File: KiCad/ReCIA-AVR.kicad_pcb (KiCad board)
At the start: 4 copper layers, 17.4 x 51.4 mm, 9 parts, among them U1 AVR128DA64-I_MR, U2 74AHCT1G17, U5 8520_DIP

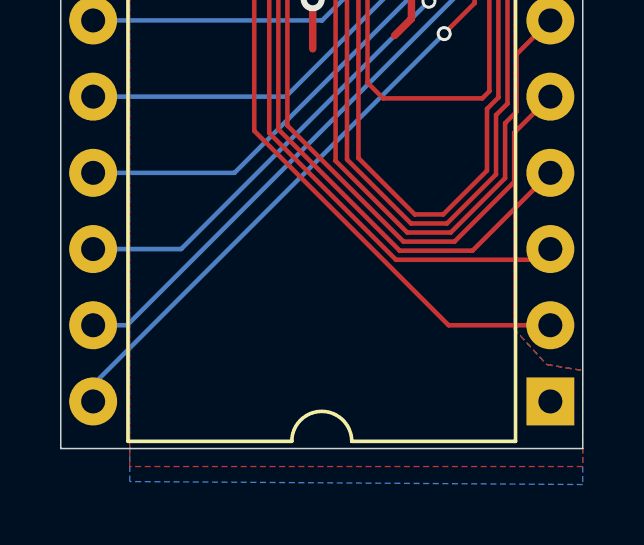
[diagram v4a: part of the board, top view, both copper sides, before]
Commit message: Add TLC2932AIPWR to the AVR version
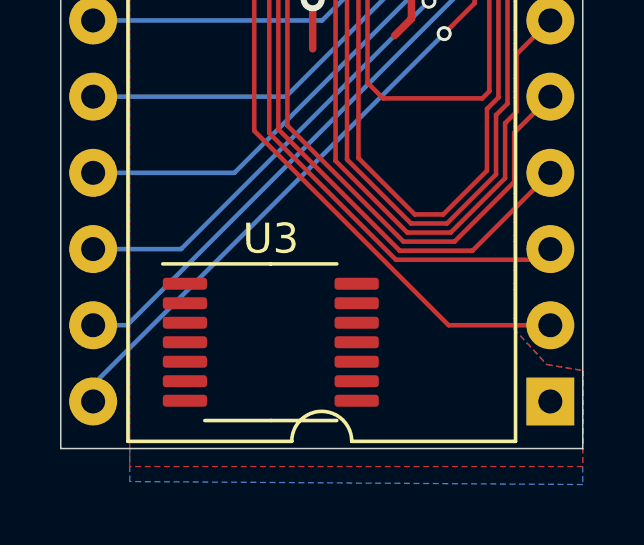
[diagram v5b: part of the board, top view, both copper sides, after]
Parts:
- added U3: TLC2932AIPWR, Package_SO:TSSOP-14_4.4x5mm_P0.65mm, F.Cu at (130.3, 105.2)
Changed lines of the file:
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@@
     (tracks 377)
     (zones 0)
-    (modules 9)
-    (nets 62)
+    (modules 10)
+    (nets 76)
   )
   (page A4)
@@
   (net 60 E)
   (net 61 /ECLK)
+  (net 62 "Net-(U3-Pad14)")
+  (net 63 "Net-(U3-Pad13)")
+  (net 64 "Net-(U3-Pad12)")
+  (net 65 "Net-(U3-Pad11)")
+  (net 66 "Net-(U3-Pad10)")
+  (net 67 "Net-(U3-Pad9)")
+  (net 68 "Net-(U3-Pad8)")
+  (net 69 "Net-(U3-Pad7)")
+  (net 70 "Net-(U3-Pad6)")
+  (net 71 "Net-(U3-Pad5)")
+  (net 72 "Net-(U3-Pad4)")
+  (net 73 "Net-(U3-Pad3)")
+  (net 74 "Net-(U3-Pad2)")
+  (net 75 "Net-(U3-Pad1)")
   (net_class Default "This is the default net class."
     (clearance 0.15)
@@
     (add_net "Net-(U1-Pad5)")
     (add_net "Net-(U2-Pad1)")
+    (add_net "Net-(U3-Pad1)")
+    (add_net "Net-(U3-Pad10)")
+    (add_net "Net-(U3-Pad11)")
+    (add_net "Net-(U3-Pad12)")
+    (add_net "Net-(U3-Pad13)")
+    (add_net "Net-(U3-Pad14)")
+    (add_net "Net-(U3-Pad2)")
+    (add_net "Net-(U3-Pad3)")
+    (add_net "Net-(U3-Pad4)")
+    (add_net "Net-(U3-Pad5)")
+    (add_net "Net-(U3-Pad6)")
+    (add_net "Net-(U3-Pad7)")
+    (add_net "Net-(U3-Pad8)")
+    (add_net "Net-(U3-Pad9)")
     (add_net PA0)
     (add_net PA1)
@@
     (add_net XTAL32K2)
   )
+  (module Package_SO:TSSOP-14_4.4x5mm_P0.65mm (layer F.Cu)
+    (at 130.302 105.156)
+    (descr "TSSOP, 14 Pin (JEDEC MO-153 Var AB-1 https://www.jedec.org/document_search?search_api_views_fulltext=MO-153), generated with kicad-footprint-generator ipc_gullwing_generator.py")
+    (tags "TSSOP SO")
+    (attr smd)
+    (fp_text reference U3 (at 0 -3.45) (layer F.SilkS)
+      (effects (font (size 1 1) (thickness 0.15)))
+    )
+    (fp_text value TLC2932AIPWR (at 0 3.45) (layer F.Fab) hide
+      (effects (font (size 1 1) (thickness 0.15)))
+    )
+    (fp_text user %R (at 0 0) (layer F.Fab) hide
+      (effects (font (size 1 1) (thickness 0.15)))
+    )
+    (fp_line (start 0 2.61) (end 2.2 2.61) (layer F.SilkS) (width 0.12))
+    (fp_line (start 0 2.61) (end -2.2 2.61) (layer F.SilkS) (width 0.12))
+    (fp_line (start 0 -2.61) (end 2.2 -2.61) (layer F.SilkS) (width 0.12))
+    (fp_line (start 0 -2.61) (end -3.6 -2.61) (layer F.SilkS) (width 0.12))
+    (fp_line (start -1.2 -2.5) (end 2.2 -2.5) (layer F.Fab) (width 0.1))
+    (fp_line (start 2.2 -2.5) (end 2.2 2.5) (layer F.Fab) (width 0.1))
+    (fp_line (start 2.2 2.5) (end -2.2 2.5) (layer F.Fab) (width 0.1))
+    (fp_line (start -2.2 2.5) (end -2.2 -1.5) (layer F.Fab) (width 0.1))
+    (fp_line (start -2.2 -1.5) (end -1.2 -2.5) (layer F.Fab) (width 0.1))
+    (fp_line (start -3.85 -2.75) (end -3.85 2.75) (layer F.CrtYd) (width 0.05))
+    (fp_line (start -3.85 2.75) (end 3.85 2.75) (layer F.CrtYd) (width 0.05))
+    (fp_line (start 3.85 2.75) (end 3.85 -2.75) (layer F.CrtYd) (width 0.05))
+    (fp_line (start 3.85 -2.75) (end -3.85 -2.75) (layer F.CrtYd) (width 0.05))
+    (pad 14 smd roundrect (at 2.8625 -1.95) (size 1.475 0.4) (layers F.Cu F.Paste F.Mask) (roundrect_rratio 0.25)
+      (net 62 "Net-(U3-Pad14)"))
+    (pad 13 smd roundrect (at 2.8625 -1.3) (size 1.475 0.4) (layers F.Cu F.Paste F.Mask) (roundrect_rratio 0.25)
+      (net 63 "Net-(U3-Pad13)"))
+    (pad 12 smd roundrect (at 2.8625 -0.65) (size 1.475 0.4) (layers F.Cu F.Paste F.Mask) (roundrect_rratio 0.25)
+      (net 64 "Net-(U3-Pad12)"))
+    (pad 11 smd roundrect (at 2.8625 0) (size 1.475 0.4) (layers F.Cu F.Paste F.Mask) (roundrect_rratio 0.25)
+      (net 65 "Net-(U3-Pad11)"))
+    (pad 10 smd roundrect (at 2.8625 0.65) (size 1.475 0.4) (layers F.Cu F.Paste F.Mask) (roundrect_rratio 0.25)
+      (net 66 "Net-(U3-Pad10)"))
+    (pad 9 smd roundrect (at 2.8625 1.3) (size 1.475 0.4) (layers F.Cu F.Paste F.Mask) (roundrect_rratio 0.25)
+      (net 67 "Net-(U3-Pad9)"))
+    (pad 8 smd roundrect (at 2.8625 1.95) (size 1.475 0.4) (layers F.Cu F.Paste F.Mask) (roundrect_rratio 0.25)
+      (net 68 "Net-(U3-Pad8)"))
+    (pad 7 smd roundrect (at -2.8625 1.95) (size 1.475 0.4) (layers F.Cu F.Paste F.Mask) (roundrect_rratio 0.25)
+      (net 69 "Net-(U3-Pad7)"))
+    (pad 6 smd roundrect (at -2.8625 1.3) (size 1.475 0.4) (layers F.Cu F.Paste F.Mask) (roundrect_rratio 0.25)
+      (net 70 "Net-(U3-Pad6)"))
+    (pad 5 smd roundrect (at -2.8625 0.65) (size 1.475 0.4) (layers F.Cu F.Paste F.Mask) (roundrect_rratio 0.25)
+      (net 71 "Net-(U3-Pad5)"))
+    (pad 4 smd roundrect (at -2.8625 0) (size 1.475 0.4) (layers F.Cu F.Paste F.Mask) (roundrect_rratio 0.25)
+      (net 72 "Net-(U3-Pad4)"))
+    (pad 3 smd roundrect (at -2.8625 -0.65) (size 1.475 0.4) (layers F.Cu F.Paste F.Mask) (roundrect_rratio 0.25)
+      (net 73 "Net-(U3-Pad3)"))
+    (pad 2 smd roundrect (at -2.8625 -1.3) (size 1.475 0.4) (layers F.Cu F.Paste F.Mask) (roundrect_rratio 0.25)
+      (net 74 "Net-(U3-Pad2)"))
+    (pad 1 smd roundrect (at -2.8625 -1.95) (size 1.475 0.4) (layers F.Cu F.Paste F.Mask) (roundrect_rratio 0.25)
+      (net 75 "Net-(U3-Pad1)"))
+    (model ${KISYS3DMOD}/Package_SO.3dshapes/TSSOP-14_4.4x5mm_P0.65mm.wrl
+      (at (xyz 0 0 0))
+      (scale (xyz 1 1 1))
+      (rotate (xyz 0 0 0))
+    )
+  )
   (module Resistor_SMD:R_0603_1608Metric_Pad0.98x0.95mm_HandSolder (layer F.Cu)
     (at 129.5 72.4 90)
@@
     (fp_text value 33 (at 0 1.43 90) (layer F.Fab) hide
       (effects (font (size 1 1) (thickness 0.15)))
-    )
-    (fp_text user %R (at 0 0 90) (layer F.Fab) hide
-      (effects (font (size 0.4 0.4) (thickness 0.06)))
     )
     (fp_line (start -0.8 0.4125) (end -0.8 -0.4125) (layer F.Fab) (width 0.1))
@@
     (fp_line (start 1.65 -0.73) (end 1.65 0.73) (layer F.CrtYd) (width 0.05))
     (fp_line (start 1.65 0.73) (end -1.65 0.73) (layer F.CrtYd) (width 0.05))
+    (fp_text user %R (at 0 0 90) (layer F.Fab) hide
+      (effects (font (size 0.4 0.4) (thickness 0.06)))
+    )
     (pad 2 smd roundrect (at 0.9125 0 90) (size 0.975 0.95) (layers F.Cu F.Paste F.Mask) (roundrect_rratio 0.25)
       (net 61 /ECLK))
@@
   (via (at 138 69.3) (size 0.8) (drill 0.4) (layers F.Cu B.Cu) (net 2))
   (via (at 138 66.8) (size 0.8) (drill 0.4) (layers F.Cu B.Cu) (net 2))
-  (via (at 130.7 73.3) (size 0.8) (drill 0.4) (layers F.Cu B.Cu) (net 28))
   (segment (start 135.25 87.55) (end 135.25 88.514) (width 0.1524) (layer F.Cu) (net 3))
   (segment (start 135.255 88.528615) (end 135.5725 88.846115) (width 0.1524) (layer F.Cu) (net 3))
@@
   (segment (start 132.75 88.3) (end 133.731 89.281) (width 0.1524) (layer F.Cu) (net 27))
   (segment (start 132.75 87.55) (end 132.75 88.3) (width 0.1524) (layer F.Cu) (net 27))
+  (via (at 130.7 73.3) (size 0.8) (drill 0.4) (layers F.Cu B.Cu) (net 28))
   (segment (start 132.25 77.75) (end 131.75 77.25) (width 0.1524) (layer F.Cu) (net 28))
   (segment (start 132.25 78.45) (end 132.25 77.75) (width 0.1524) (layer F.Cu) (net 28))

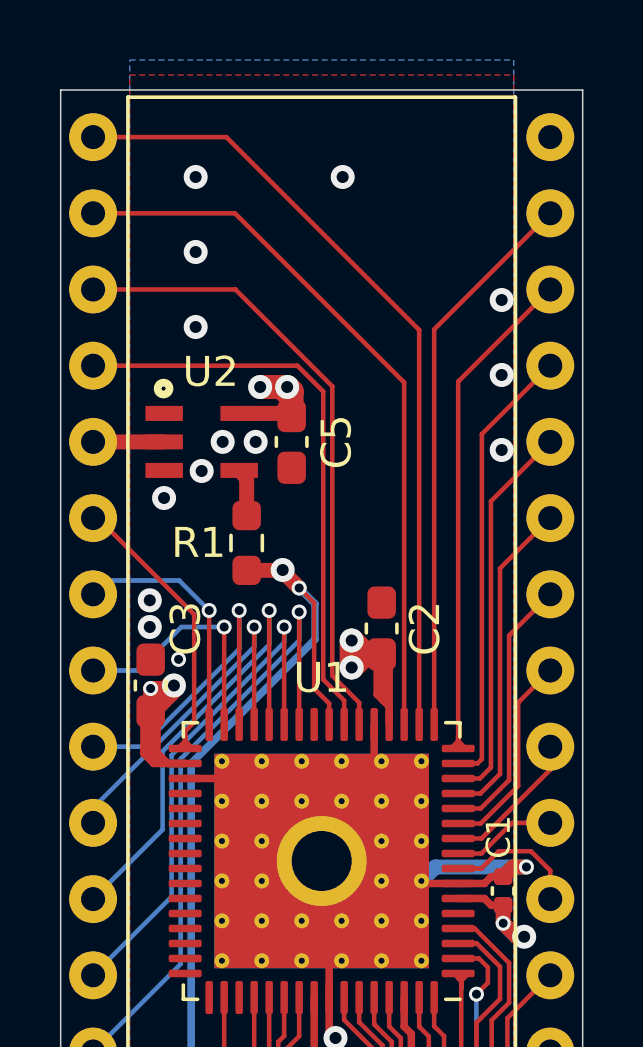
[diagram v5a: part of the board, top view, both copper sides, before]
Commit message: Add 10uF 1206 capacitor on VCC input for the AVR version
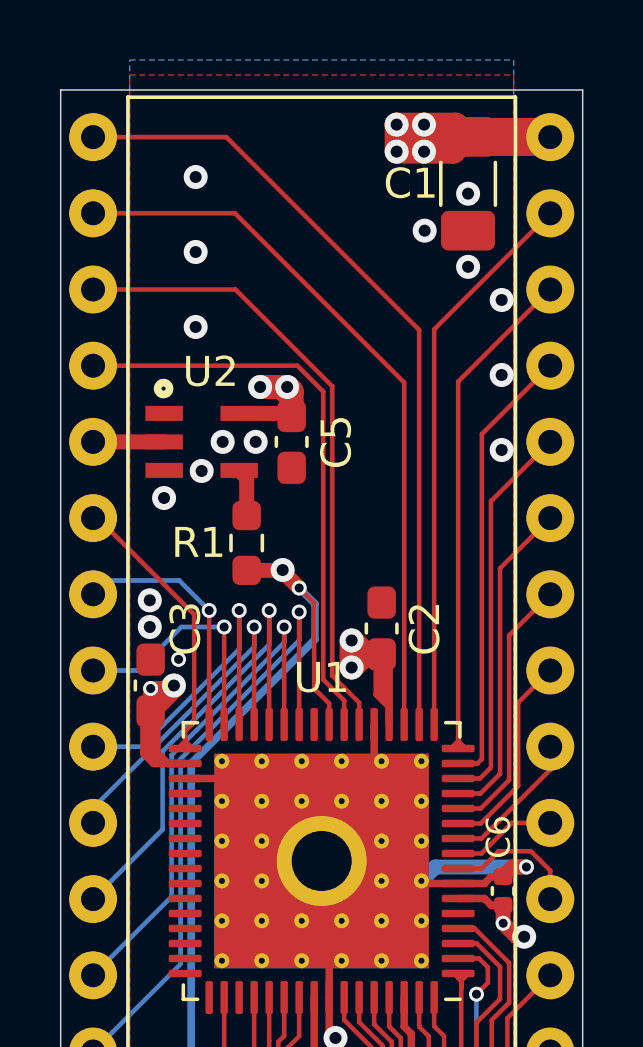
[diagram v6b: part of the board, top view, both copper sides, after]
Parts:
- added C1: C, Capacitor_SMD:C_1206_3216Metric_Pad1.33x1.80mm_HandSolder, F.Cu at (136.9, 60.4)
- renumbered C1 to C6
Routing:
- net VCC: track 38.4 -> 49.8 mm, vias 10 -> 14
- net GND: vias 18 -> 20
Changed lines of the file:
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@@
     (thickness 1.6)
     (drawings 4)
-    (tracks 377)
+    (tracks 396)
     (zones 0)
-    (modules 10)
+    (modules 11)
     (nets 76)
   )
@@
     (add_net XTAL32K2)
   )
+  (module Capacitor_SMD:C_1206_3216Metric_Pad1.33x1.80mm_HandSolder (layer F.Cu)
+    (at 136.8806 60.4266 270)
+    (descr "Capacitor SMD 1206 (3216 Metric), square (rectangular) end terminal, IPC_7351 nominal with elongated pad for handsoldering. (Body size source: IPC-SM-782 page 76, https://www.pcb-3d.com/wordpress/wp-content/uploads/ipc-sm-782a_amendment_1_and_2.pdf), generated with kicad-footprint-generator")
+    (tags "capacitor handsolder")
+    (attr smd)
+    (fp_text reference C1 (at 0 1.905 180) (layer F.SilkS)
+      (effects (font (size 1 1) (thickness 0.15)))
+    )
+    (fp_text value C (at 0 1.85 90) (layer F.Fab) hide
+      (effects (font (size 1 1) (thickness 0.15)))
+    )
+    (fp_line (start 2.48 1.15) (end -2.48 1.15) (layer F.CrtYd) (width 0.05))
+    (fp_line (start 2.48 -1.15) (end 2.48 1.15) (layer F.CrtYd) (width 0.05))
+    (fp_line (start -2.48 -1.15) (end 2.48 -1.15) (layer F.CrtYd) (width 0.05))
+    (fp_line (start -2.48 1.15) (end -2.48 -1.15) (layer F.CrtYd) (width 0.05))
+    (fp_line (start -0.711252 0.91) (end 0.711252 0.91) (layer F.SilkS) (width 0.12))
+    (fp_line (start -0.711252 -0.91) (end 0.711252 -0.91) (layer F.SilkS) (width 0.12))
+    (fp_line (start 1.6 0.8) (end -1.6 0.8) (layer F.Fab) (width 0.1))
+    (fp_line (start 1.6 -0.8) (end 1.6 0.8) (layer F.Fab) (width 0.1))
+    (fp_line (start -1.6 -0.8) (end 1.6 -0.8) (layer F.Fab) (width 0.1))
+    (fp_line (start -1.6 0.8) (end -1.6 -0.8) (layer F.Fab) (width 0.1))
+    (fp_text user %R (at 0 0 90) (layer F.Fab) hide
+      (effects (font (size 0.8 0.8) (thickness 0.12)))
+    )
+    (pad 2 smd roundrect (at 1.5625 0 270) (size 1.325 1.8) (layers F.Cu F.Paste F.Mask) (roundrect_rratio 0.188679)
+      (net 2 GND))
+    (pad 1 smd roundrect (at -1.5625 0 270) (size 1.325 1.8) (layers F.Cu F.Paste F.Mask) (roundrect_rratio 0.188679)
+      (net 1 VCC))
+    (model ${KISYS3DMOD}/Capacitor_SMD.3dshapes/C_1206_3216Metric.wrl
+      (at (xyz 0 0 0))
+      (scale (xyz 1 1 1))
+      (rotate (xyz 0 0 0))
+    )
+  )
   (module Package_SO:TSSOP-14_4.4x5mm_P0.65mm (layer F.Cu)
     (at 130.302 105.156)
@@
     )
     (fp_text value TLC2932AIPWR (at 0 3.45) (layer F.Fab) hide
-      (effects (font (size 1 1) (thickness 0.15)))
-    )
-    (fp_text user %R (at 0 0) (layer F.Fab) hide
       (effects (font (size 1 1) (thickness 0.15)))
     )
@@
     (fp_line (start 3.85 2.75) (end 3.85 -2.75) (layer F.CrtYd) (width 0.05))
     (fp_line (start 3.85 -2.75) (end -3.85 -2.75) (layer F.CrtYd) (width 0.05))
+    (fp_text user %R (at 0 0) (layer F.Fab) hide
+      (effects (font (size 1 1) (thickness 0.15)))
+    )
     (pad 14 smd roundrect (at 2.8625 -1.95) (size 1.475 0.4) (layers F.Cu F.Paste F.Mask) (roundrect_rratio 0.25)
       (net 62 "Net-(U3-Pad14)"))
@@
     (tags capacitor)
     (attr smd)
-    (fp_text reference C1 (at 1.8 -0.15 90) (layer F.SilkS)
+    (fp_text reference C6 (at 1.8 -0.15 90) (layer F.SilkS)
       (effects (font (size 0.8 0.8) (thickness 0.15)))
     )
@@
   (segment (start 127.075 77.15) (end 126.975 77.25) (width 0.5) (layer F.Cu) (net 1))
   (segment (start 126.3 77.25) (end 126.3 78.0125) (width 0.5) (layer F.Cu) (net 1))
+  (segment (start 136.6715 58.87) (end 136.652 58.8895) (width 1.27) (layer F.Cu) (net 1))
+  (segment (start 139.6141 58.8641) (end 139.62 58.87) (width 1.27) (layer F.Cu) (net 1))
+  (segment (start 136.8806 58.8641) (end 139.6141 58.8641) (width 1.27) (layer F.Cu) (net 1))
+  (via (at 135.413 59.3542) (size 0.8) (drill 0.4) (layers F.Cu B.Cu) (net 1))
+  (via (at 135.413 58.4542) (size 0.8) (drill 0.4) (layers F.Cu B.Cu) (net 1))
+  (via (at 134.4986 58.4542) (size 0.8) (drill 0.4) (layers F.Cu B.Cu) (net 1))
+  (via (at 134.4986 59.3542) (size 0.8) (drill 0.4) (layers F.Cu B.Cu) (net 1))
+  (segment (start 134.4986 58.4542) (end 135.413 58.4542) (width 0.8) (layer F.Cu) (net 1))
+  (segment (start 136.4707 58.4542) (end 136.8806 58.8641) (width 0.8) (layer F.Cu) (net 1))
+  (segment (start 135.413 58.4542) (end 136.4707 58.4542) (width 0.8) (layer F.Cu) (net 1))
+  (segment (start 134.4986 58.4542) (end 134.4986 59.3542) (width 0.8) (layer F.Cu) (net 1))
+  (segment (start 134.4986 59.3542) (end 135.413 59.3542) (width 0.8) (layer F.Cu) (net 1))
+  (segment (start 136.3905 59.3542) (end 136.8806 58.8641) (width 0.8) (layer F.Cu) (net 1))
+  (segment (start 135.413 59.3542) (end 136.3905 59.3542) (width 0.8) (layer F.Cu) (net 1))
+  (segment (start 134.4986 58.4542) (end 134.9978 58.9534) (width 0.8) (layer F.Cu) (net 1))
+  (segment (start 136.7913 58.9534) (end 136.8806 58.8641) (width 0.8) (layer F.Cu) (net 1))
+  (segment (start 134.9978 58.9534) (end 136.7913 58.9534) (width 0.8) (layer F.Cu) (net 1))
   (via (at 132.461 88.9) (size 0.8) (drill 0.4) (layers F.Cu B.Cu) (net 2))
   (via (at 138.825 83.2) (size 0.5) (drill 0.3) (layers F.Cu B.Cu) (net 2))
@@
   (via (at 127.8 62.7) (size 0.8) (drill 0.4) (layers F.Cu B.Cu) (net 2))
   (via (at 127.8 60.2) (size 0.8) (drill 0.4) (layers F.Cu B.Cu) (net 2))
-  (via (at 132.7 60.2) (size 0.8) (drill 0.4) (layers F.Cu B.Cu) (net 2))
+  (via (at 136.8806 60.7568) (size 0.8) (drill 0.4) (layers F.Cu B.Cu) (net 2))
   (via (at 129.8 69.03) (size 0.8) (drill 0.4) (layers F.Cu B.Cu) (net 2))
   (via (at 128.7 69.03) (size 0.8) (drill 0.4) (layers F.Cu B.Cu) (net 2))
@@
   (via (at 138 69.3) (size 0.8) (drill 0.4) (layers F.Cu B.Cu) (net 2))
   (via (at 138 66.8) (size 0.8) (drill 0.4) (layers F.Cu B.Cu) (net 2))
+  (via (at 136.8806 63.1952) (size 0.8) (drill 0.4) (layers F.Cu B.Cu) (net 2))
+  (via (at 135.4328 61.9887) (size 0.8) (drill 0.4) (layers F.Cu B.Cu) (net 2))
   (segment (start 135.25 87.55) (end 135.25 88.514) (width 0.1524) (layer F.Cu) (net 3))
   (segment (start 135.255 88.528615) (end 135.5725 88.846115) (width 0.1524) (layer F.Cu) (net 3))

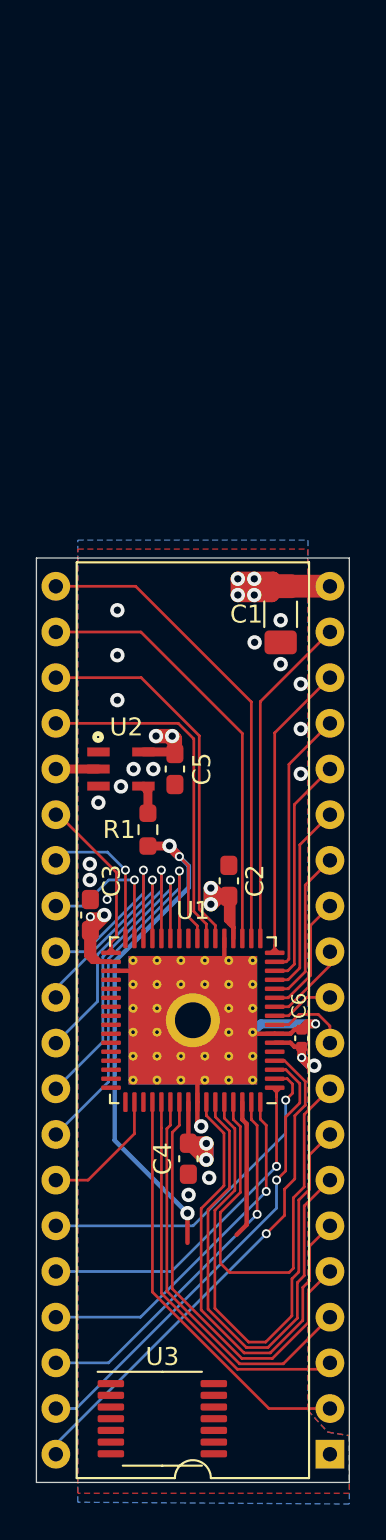
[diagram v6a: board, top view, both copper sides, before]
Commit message: Fixed placement of PLL-chip and added inductor and caps for power supply pins Logic VDD and VCO VDD for the AVR-version
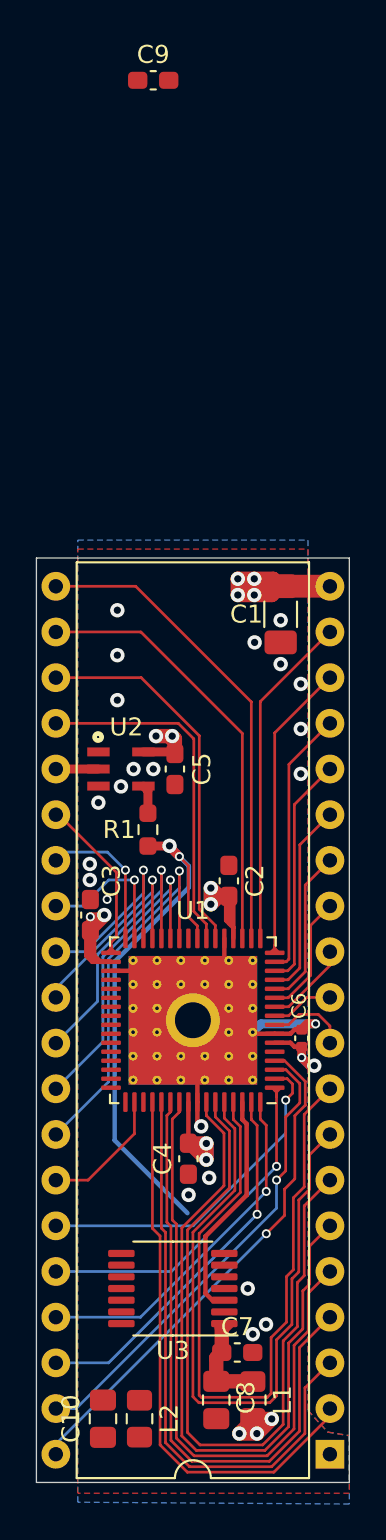
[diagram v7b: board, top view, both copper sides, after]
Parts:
- added C10: 10uF, Capacitor_SMD:C_0805_2012Metric_Pad1.18x1.45mm_HandSolder, F.Cu at (127.0, 105.2)
- added C7: 0.01uF, Capacitor_SMD:C_0603_1608Metric_Pad1.08x0.95mm_HandSolder, F.Cu at (134.5, 101.5)
- added C8: 10uF, Capacitor_SMD:C_0805_2012Metric_Pad1.18x1.45mm_HandSolder, F.Cu at (133.3, 104.1)
- added C9: 0.01uF, Capacitor_SMD:C_0603_1608Metric_Pad1.08x0.95mm_HandSolder, F.Cu at (129.8, 30.7)
- added L1: 100uH, Inductor_SMD:L_0805_2012Metric_Pad1.15x1.40mm_HandSolder, F.Cu at (135.3, 104.1)
- added L2: 100uH, Inductor_SMD:L_0805_2012Metric_Pad1.15x1.40mm_HandSolder, F.Cu at (129.0, 105.2)
- moved U3 7.26 mm to (130.9, 97.9), turned to 180 degrees
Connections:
- U3 pad 1: Net-(U3-Pad1) -> /LOGIC_VDD
- U3 pad 10: Net-(U3-Pad10) -> GND
- U3 pad 11: Net-(U3-Pad11) -> GND
- U3 pad 14: Net-(U3-Pad14) -> /VCO_VDD
- U3 pad 3: Net-(U3-Pad3) -> EXTCLK
- U3 pad 4: Net-(U3-Pad4) -> E-CLK
- U3 pad 7: Net-(U3-Pad7) -> GND
- U3 pad 8: Net-(U3-Pad8) -> GND
- U3 pad 9: Net-(U3-Pad9) -> GND
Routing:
- net PA7: track 24.8 -> 39.8 mm
- net PA5: track 27.3 -> 40.4 mm
- net PA4: track 25.8 -> 38.9 mm
- net PA3: track 23.9 -> 36.1 mm
- net PA2: track 22.4 -> 34.4 mm
- net PA1: track 21.9 -> 32.6 mm
- net PA6: track 28.8 -> 38.3 mm
- net PA0: track 23.1 -> 31.0 mm
- net /LOGIC_VDD: track 0.00 -> 7.55 mm
- net EXTCLK: track 7.71 -> 12.9 mm
- net VCC: track 49.8 -> 54.2 mm, vias 14 -> 17
- net E-CLK: track 34.9 -> 33.2 mm
- net GND: vias 20 -> 22
